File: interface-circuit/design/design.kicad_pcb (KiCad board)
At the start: 2 copper layers, 126.8 x 83.8 mm, 23 parts, among them J10 FAN_RELAY, J11 Conn_Switch, J12 Conn_Reset, J2 Screw_Term_RPi, J3 Screw_Term_Detector, J4 12V_IN, J5 Conn_Pwr_LED, J6 Conn_Piezo, J7 Conn_Printer_Mode, J8 Conn_Fan_Mode, J9 PRINTER_RELAY, Q1 2N3904-AP, Q2 2N3904-AP, Q3 2N3904-AP, U1 LogicLevelConverter_BOB-08745

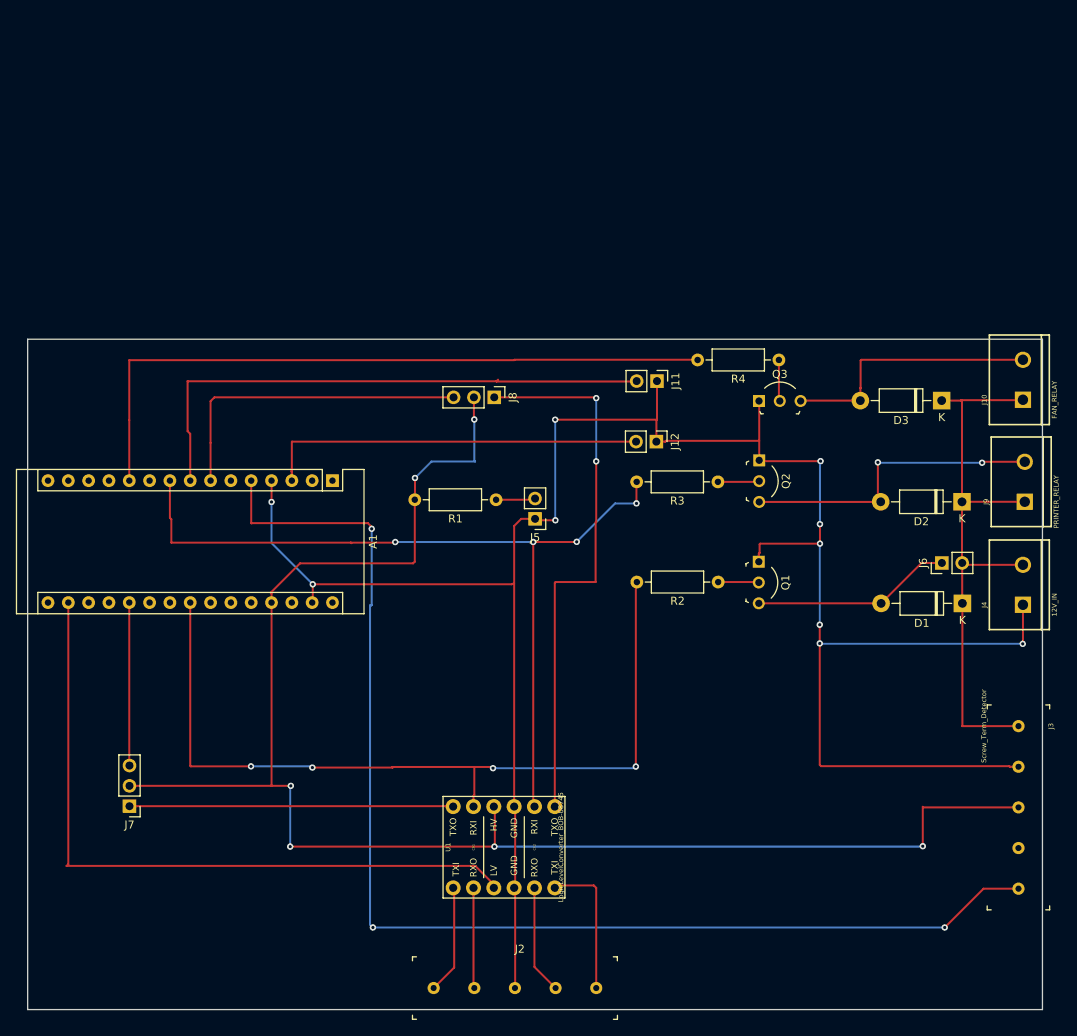
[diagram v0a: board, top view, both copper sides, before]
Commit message: Updated protoboard layout to match rough implementation
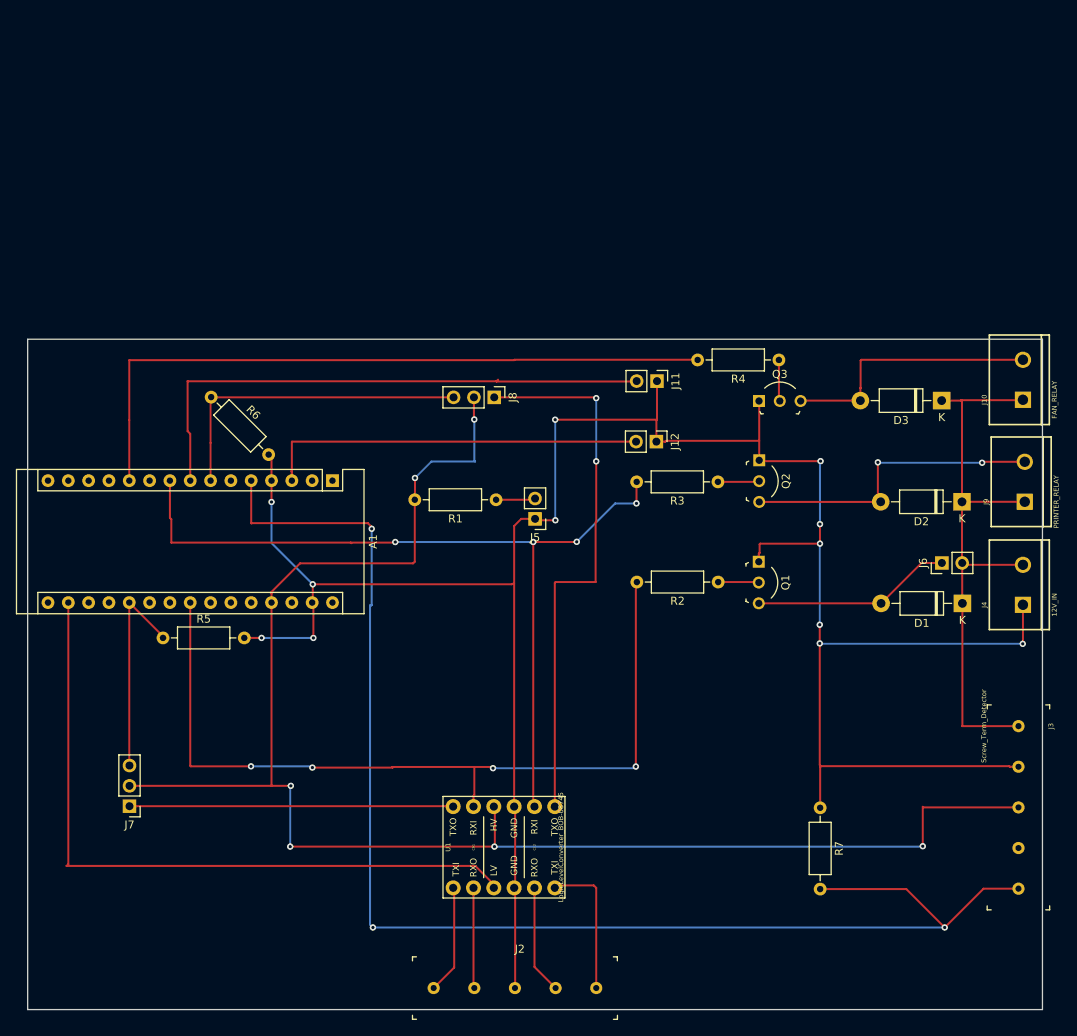
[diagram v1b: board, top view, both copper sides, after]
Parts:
- added R5: 10R, Resistor_THT:R_Axial_DIN0207_L6.3mm_D2.5mm_P10.16mm_Horizontal, F.Cu at (39.8, 113.5)
- added R6: 10R, Resistor_THT:R_Axial_DIN0207_L6.3mm_D2.5mm_P10.16mm_Horizontal, F.Cu at (45.8, 83.4)
- added R7: 10R, Resistor_THT:R_Axial_DIN0207_L6.3mm_D2.5mm_P10.16mm_Horizontal, F.Cu at (122.0, 134.7)
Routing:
- net GND: track 270.5 -> 292.2 mm, vias 10 -> 12
- net /DETECTOR_SIGNAL: track 153.9 -> 171.4 mm
- net /SW_PRINTER_RELAY: track 20.4 -> 26.5 mm
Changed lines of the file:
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@@
     (thickness 1.6)
     (drawings 4)
-    (tracks 260)
+    (tracks 274)
     (zones 0)
-    (modules 23)
+    (modules 26)
     (nets 26)
   )
@@
     (add_net "Net-(Q2-Pad2)")
     (add_net "Net-(Q3-Pad2)")
+  )
+  (module Resistor_THT:R_Axial_DIN0207_L6.3mm_D2.5mm_P10.16mm_Horizontal (layer F.Cu)
+    (at 121.9708 134.747 270)
+    (descr "Resistor, Axial_DIN0207 series, Axial, Horizontal, pin pitch=10.16mm, 0.25W = 1/4W, length*diameter=6.3*2.5mm^2, http://cdn-reichelt.de/documents/datenblatt/B400/1_4W%23YAG.pdf")
+    (tags "Resistor Axial_DIN0207 series Axial Horizontal pin pitch 10.16mm 0.25W = 1/4W length 6.3mm diameter 2.5mm")
+    (fp_text reference R7 (at 5.08 -2.37 90) (layer F.SilkS)
+      (effects (font (size 1 1) (thickness 0.15)))
+    )
+    (fp_text value 10R (at 5.08 2.37 90) (layer F.Fab)
+      (effects (font (size 1 1) (thickness 0.15)))
+    )
+    (fp_text user %R (at 5.08 0 90) (layer F.Fab)
+      (effects (font (size 1 1) (thickness 0.15)))
+    )
+    (fp_line (start 11.21 -1.5) (end -1.05 -1.5) (layer F.CrtYd) (width 0.05))
+    (fp_line (start 11.21 1.5) (end 11.21 -1.5) (layer F.CrtYd) (width 0.05))
+    (fp_line (start -1.05 1.5) (end 11.21 1.5) (layer F.CrtYd) (width 0.05))
+    (fp_line (start -1.05 -1.5) (end -1.05 1.5) (layer F.CrtYd) (width 0.05))
+    (fp_line (start 9.12 0) (end 8.35 0) (layer F.SilkS) (width 0.12))
+    (fp_line (start 1.04 0) (end 1.81 0) (layer F.SilkS) (width 0.12))
+    (fp_line (start 8.35 -1.37) (end 1.81 -1.37) (layer F.SilkS) (width 0.12))
+    (fp_line (start 8.35 1.37) (end 8.35 -1.37) (layer F.SilkS) (width 0.12))
+    (fp_line (start 1.81 1.37) (end 8.35 1.37) (layer F.SilkS) (width 0.12))
+    (fp_line (start 1.81 -1.37) (end 1.81 1.37) (layer F.SilkS) (width 0.12))
+    (fp_line (start 10.16 0) (end 8.23 0) (layer F.Fab) (width 0.1))
+    (fp_line (start 0 0) (end 1.93 0) (layer F.Fab) (width 0.1))
+    (fp_line (start 8.23 -1.25) (end 1.93 -1.25) (layer F.Fab) (width 0.1))
+    (fp_line (start 8.23 1.25) (end 8.23 -1.25) (layer F.Fab) (width 0.1))
+    (fp_line (start 1.93 1.25) (end 8.23 1.25) (layer F.Fab) (width 0.1))
+    (fp_line (start 1.93 -1.25) (end 1.93 1.25) (layer F.Fab) (width 0.1))
+    (pad 2 thru_hole oval (at 10.16 0 270) (size 1.6 1.6) (drill 0.8) (layers *.Cu *.Mask)
+      (net 4 /DETECTOR_SIGNAL))
+    (pad 1 thru_hole circle (at 0 0 270) (size 1.6 1.6) (drill 0.8) (layers *.Cu *.Mask)
+      (net 3 GND))
+    (model ${KISYS3DMOD}/Resistor_THT.3dshapes/R_Axial_DIN0207_L6.3mm_D2.5mm_P10.16mm_Horizontal.wrl
+      (at (xyz 0 0 0))
+      (scale (xyz 1 1 1))
+      (rotate (xyz 0 0 0))
+    )
+  )
+  (module Resistor_THT:R_Axial_DIN0207_L6.3mm_D2.5mm_P10.16mm_Horizontal (layer F.Cu)
+    (at 45.847 83.4136 315)
+    (descr "Resistor, Axial_DIN0207 series, Axial, Horizontal, pin pitch=10.16mm, 0.25W = 1/4W, length*diameter=6.3*2.5mm^2, http://cdn-reichelt.de/documents/datenblatt/B400/1_4W%23YAG.pdf")
+    (tags "Resistor Axial_DIN0207 series Axial Horizontal pin pitch 10.16mm 0.25W = 1/4W length 6.3mm diameter 2.5mm")
+    (fp_text reference R6 (at 5.08 -2.37 135) (layer F.SilkS)
+      (effects (font (size 1 1) (thickness 0.15)))
+    )
+    (fp_text value 10R (at 5.08 2.37 135) (layer F.Fab)
+      (effects (font (size 1 1) (thickness 0.15)))
+    )
+    (fp_text user %R (at 5.08 0 135) (layer F.Fab)
+      (effects (font (size 1 1) (thickness 0.15)))
+    )
+    (fp_line (start 11.21 -1.5) (end -1.05 -1.5) (layer F.CrtYd) (width 0.05))
+    (fp_line (start 11.21 1.5) (end 11.21 -1.5) (layer F.CrtYd) (width 0.05))
+    (fp_line (start -1.05 1.5) (end 11.21 1.5) (layer F.CrtYd) (width 0.05))
+    (fp_line (start -1.05 -1.5) (end -1.05 1.5) (layer F.CrtYd) (width 0.05))
+    (fp_line (start 9.12 0) (end 8.35 0) (layer F.SilkS) (width 0.12))
+    (fp_line (start 1.04 0) (end 1.81 0) (layer F.SilkS) (width 0.12))
+    (fp_line (start 8.35 -1.37) (end 1.81 -1.37) (layer F.SilkS) (width 0.12))
+    (fp_line (start 8.35 1.37) (end 8.35 -1.37) (layer F.SilkS) (width 0.12))
+    (fp_line (start 1.81 1.37) (end 8.35 1.37) (layer F.SilkS) (width 0.12))
+    (fp_line (start 1.81 -1.37) (end 1.81 1.37) (layer F.SilkS) (width 0.12))
+    (fp_line (start 10.16 0) (end 8.23 0) (layer F.Fab) (width 0.1))
+    (fp_line (start 0 0) (end 1.93 0) (layer F.Fab) (width 0.1))
+    (fp_line (start 8.23 -1.25) (end 1.93 -1.25) (layer F.Fab) (width 0.1))
+    (fp_line (start 8.23 1.25) (end 8.23 -1.25) (layer F.Fab) (width 0.1))
+    (fp_line (start 1.93 1.25) (end 8.23 1.25) (layer F.Fab) (width 0.1))
+    (fp_line (start 1.93 -1.25) (end 1.93 1.25) (layer F.Fab) (width 0.1))
+    (pad 2 thru_hole oval (at 10.16 0 315) (size 1.6 1.6) (drill 0.8) (layers *.Cu *.Mask)
+      (net 3 GND))
+    (pad 1 thru_hole circle (at 0 0 315) (size 1.6 1.6) (drill 0.8) (layers *.Cu *.Mask)
+      (net 21 /SW_FAN_RELAY))
+    (model ${KISYS3DMOD}/Resistor_THT.3dshapes/R_Axial_DIN0207_L6.3mm_D2.5mm_P10.16mm_Horizontal.wrl
+      (at (xyz 0 0 0))
+      (scale (xyz 1 1 1))
+      (rotate (xyz 0 0 0))
+    )
+  )
+  (module Resistor_THT:R_Axial_DIN0207_L6.3mm_D2.5mm_P10.16mm_Horizontal (layer F.Cu)
+    (at 39.8272 113.5126)
+    (descr "Resistor, Axial_DIN0207 series, Axial, Horizontal, pin pitch=10.16mm, 0.25W = 1/4W, length*diameter=6.3*2.5mm^2, http://cdn-reichelt.de/documents/datenblatt/B400/1_4W%23YAG.pdf")
+    (tags "Resistor Axial_DIN0207 series Axial Horizontal pin pitch 10.16mm 0.25W = 1/4W length 6.3mm diameter 2.5mm")
+    (fp_text reference R5 (at 5.08 -2.37) (layer F.SilkS)
+      (effects (font (size 1 1) (thickness 0.15)))
+    )
+    (fp_text value 10R (at 5.08 2.37) (layer F.Fab)
+      (effects (font (size 1 1) (thickness 0.15)))
+    )
+    (fp_text user %R (at 5.08 0) (layer F.Fab)
+      (effects (font (size 1 1) (thickness 0.15)))
+    )
+    (fp_line (start 11.21 -1.5) (end -1.05 -1.5) (layer F.CrtYd) (width 0.05))
+    (fp_line (start 11.21 1.5) (end 11.21 -1.5) (layer F.CrtYd) (width 0.05))
+    (fp_line (start -1.05 1.5) (end 11.21 1.5) (layer F.CrtYd) (width 0.05))
+    (fp_line (start -1.05 -1.5) (end -1.05 1.5) (layer F.CrtYd) (width 0.05))
+    (fp_line (start 9.12 0) (end 8.35 0) (layer F.SilkS) (width 0.12))
+    (fp_line (start 1.04 0) (end 1.81 0) (layer F.SilkS) (width 0.12))
+    (fp_line (start 8.35 -1.37) (end 1.81 -1.37) (layer F.SilkS) (width 0.12))
+    (fp_line (start 8.35 1.37) (end 8.35 -1.37) (layer F.SilkS) (width 0.12))
+    (fp_line (start 1.81 1.37) (end 8.35 1.37) (layer F.SilkS) (width 0.12))
+    (fp_line (start 1.81 -1.37) (end 1.81 1.37) (layer F.SilkS) (width 0.12))
+    (fp_line (start 10.16 0) (end 8.23 0) (layer F.Fab) (width 0.1))
+    (fp_line (start 0 0) (end 1.93 0) (layer F.Fab) (width 0.1))
+    (fp_line (start 8.23 -1.25) (end 1.93 -1.25) (layer F.Fab) (width 0.1))
+    (fp_line (start 8.23 1.25) (end 8.23 -1.25) (layer F.Fab) (width 0.1))
+    (fp_line (start 1.93 1.25) (end 8.23 1.25) (layer F.Fab) (width 0.1))
+    (fp_line (start 1.93 -1.25) (end 1.93 1.25) (layer F.Fab) (width 0.1))
+    (pad 2 thru_hole oval (at 10.16 0) (size 1.6 1.6) (drill 0.8) (layers *.Cu *.Mask)
+      (net 3 GND))
+    (pad 1 thru_hole circle (at 0 0) (size 1.6 1.6) (drill 0.8) (layers *.Cu *.Mask)
+      (net 25 /SW_PRINTER_RELAY))
+    (model ${KISYS3DMOD}/Resistor_THT.3dshapes/R_Axial_DIN0207_L6.3mm_D2.5mm_P10.16mm_Horizontal.wrl
+      (at (xyz 0 0 0))
+      (scale (xyz 1 1 1))
+      (rotate (xyz 0 0 0))
+    )
   )
   (module Module:Arduino_Nano (layer F.Cu)
@@
   (segment (start 53.3908 96.52) (end 53.3908 101.6508) (width 0.25) (layer B.Cu) (net 3))
   (segment (start 53.3908 101.6508) (end 58.547 106.807) (width 0.25) (layer B.Cu) (net 3))
+  (segment (start 121.9708 129.6416) (end 122.0724 129.54) (width 0.25) (layer F.Cu) (net 3))
+  (segment (start 121.9708 134.747) (end 121.9708 129.6416) (width 0.25) (layer F.Cu) (net 3))
+  (via (at 52.1462 113.5126) (size 0.8) (drill 0.4) (layers F.Cu B.Cu) (net 3))
+  (segment (start 49.9872 113.5126) (end 52.1462 113.5126) (width 0.25) (layer F.Cu) (net 3))
+  (via (at 58.6232 113.5126) (size 0.8) (drill 0.4) (layers F.Cu B.Cu) (net 3))
+  (segment (start 52.1462 113.5126) (end 58.6232 113.5126) (width 0.25) (layer B.Cu) (net 3))
+  (segment (start 58.6232 109.2454) (end 58.4708 109.093) (width 0.25) (layer F.Cu) (net 3))
+  (segment (start 58.6232 113.5126) (end 58.6232 109.2454) (width 0.25) (layer F.Cu) (net 3))
+  (segment (start 53.3908 90.9574) (end 53.031205 90.597805) (width 0.25) (layer F.Cu) (net 3))
+  (segment (start 53.3908 93.853) (end 53.3908 90.9574) (width 0.25) (layer F.Cu) (net 3))
   (segment (start 146.7612 144.8562) (end 142.3924 144.8562) (width 0.25) (layer F.Cu) (net 4))
   (via (at 137.541 149.7076) (size 0.8) (drill 0.4) (layers F.Cu B.Cu) (net 4))
@@
   (segment (start 65.7098 109.3724) (end 65.7098 109.601) (width 0.25) (layer B.Cu) (net 4))
   (segment (start 65.7098 109.601) (end 65.7098 149.352) (width 0.25) (layer B.Cu) (net 4))
+  (segment (start 132.7404 144.907) (end 137.541 149.7076) (width 0.25) (layer F.Cu) (net 4))
+  (segment (start 121.9708 144.907) (end 132.7404 144.907) (width 0.25) (layer F.Cu) (net 4))
   (segment (start 76.1492 134.2136) (end 76.2254 134.2898) (width 0.25) (layer B.Cu) (net 5))
   (segment (start 76.0476 134.5438) (end 76.0984 134.5946) (width 0.25) (layer F.Cu) (net 5))
@@
   (segment (start 35.6108 129.4384) (end 35.6362 129.4638) (width 0.25) (layer F.Cu) (net 25))
   (segment (start 35.6108 109.093) (end 35.6108 129.4384) (width 0.25) (layer F.Cu) (net 25))
+  (segment (start 39.8272 113.3094) (end 39.8272 113.5126) (width 0.25) (layer F.Cu) (net 25))
+  (segment (start 35.6108 109.093) (end 39.8272 113.3094) (width 0.25) (layer F.Cu) (net 25))
 )

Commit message: Adding license
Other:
- board text added: "Arduino 3d printer cut off program Copyright (C) 2019 Christopher Speck This program is free software: you can redistribute it and/or modify it under the terms of the GNU General Public License as published by the Free Software Foundation, either version 3 of the License, or (at your option) any later version. This program is distributed in the hope that it will be useful, but WITHOUT ANY WARRANT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"
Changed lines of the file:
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@@
   (general
     (thickness 1.6)
-    (drawings 4)
+    (drawings 5)
     (tracks 274)
     (zones 0)
@@
       (net 16 /LV_FanPowerDemand) (solder_mask_margin 0.1016))
   )
+  (gr_text "Arduino 3d printer cut off program\nCopyright (C) 2019 Christopher Speck\n\nThis program is free software: you can redistribute it and/or modify\nit under the terms of the GNU General Public License as published by\nthe Free Software Foundation, either version 3 of the License, or\n(at your option) any later version.\n\nThis program is distributed in the hope that it will be useful,\nbut WITHOUT ANY WARRANTY; without even the implied warranty of\nMERCHANTABILITY or FITNESS FOR A PARTICULAR PURPOSE.  See the\nGNU General Public License for more details.\n\nYou should have received a copy of the GNU General Public License\nalong with this program.  If not, see <https://www.gnu.org/licenses/>." (at 79.8068 54.229) (layer F.Cu)
+    (effects (font (size 1.5 1.5) (thickness 0.3)))
+  )
   (gr_line (start 22.9108 159.9692) (end 22.9108 76.1746) (layer Edge.Cuts) (width 0.05))
